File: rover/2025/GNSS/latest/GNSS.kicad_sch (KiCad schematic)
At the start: 34 parts, among them J1 Eth-Horiz, J2 Eth-Horiz, J4 JST6_Pin, J5 USB_C_USB4145-GCT, SW1 TS09-63-25-WT-160-SMT-TR, SW2 TS09-63-25-WT-160-SMT-TR, U1 SN65HVD232, U2 ESP32-S3-WROVER, U3 LDO-LM7805MPX/NOPB, U4 LDO-TLV74033PDBVR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

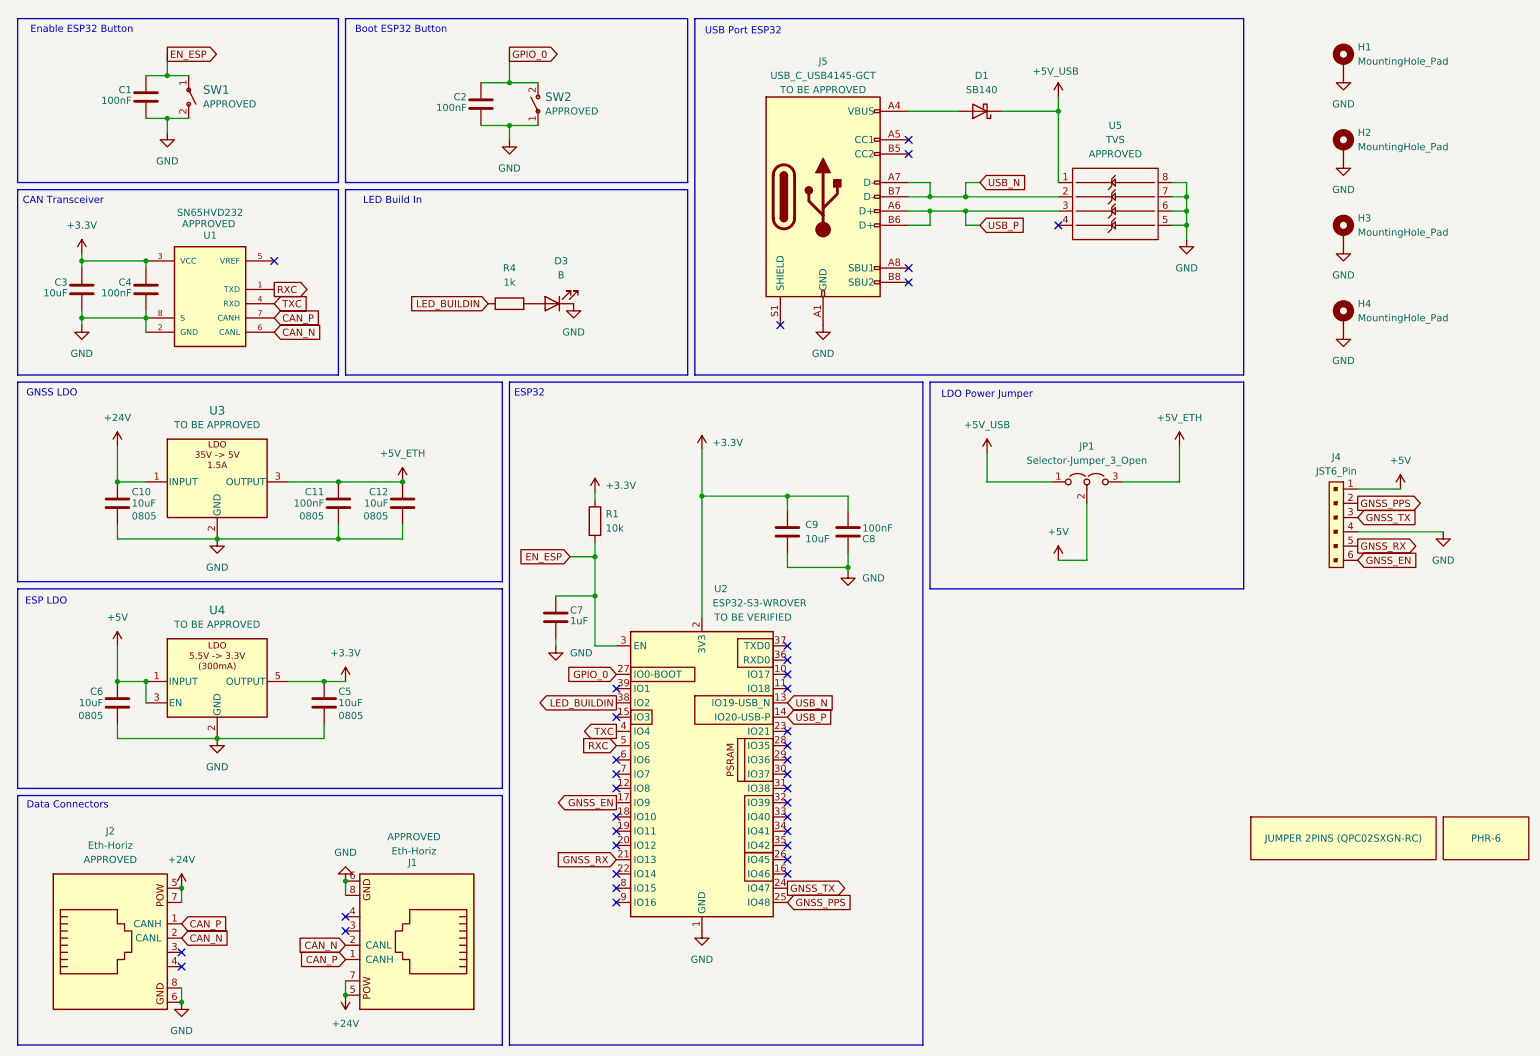
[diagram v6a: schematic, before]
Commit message: GNSS power bug fix
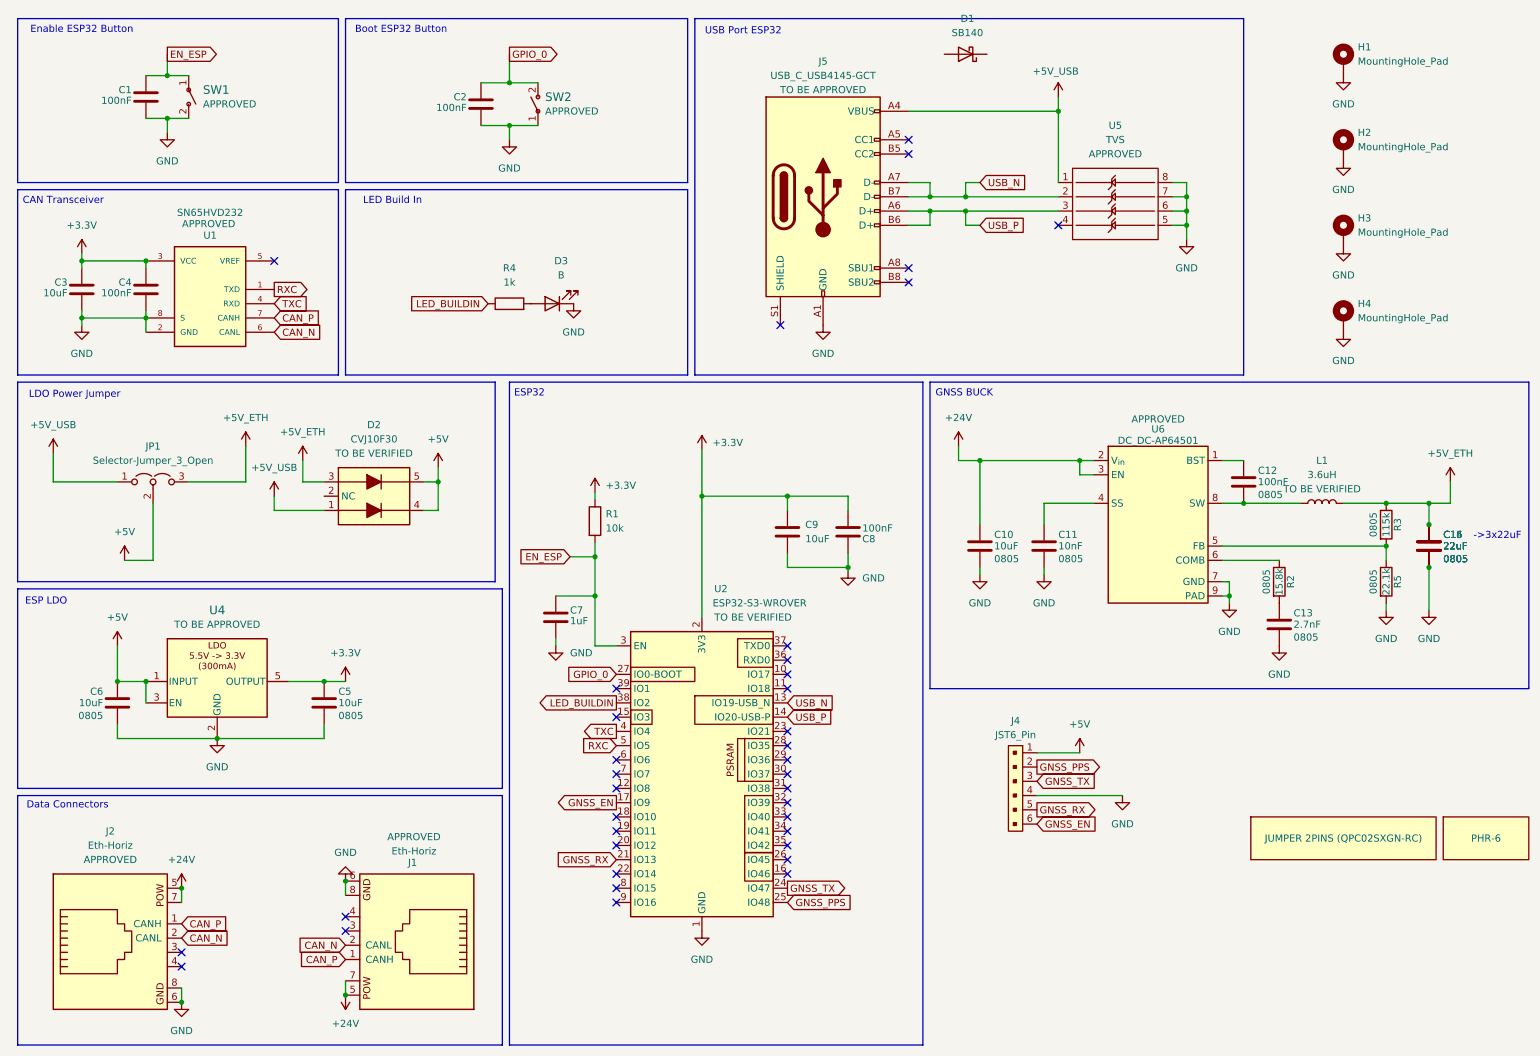
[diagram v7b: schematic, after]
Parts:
- removed C11: 100nF, Capacitor_SMD:C_0805_2012Metric_Pad1.18x1.45mm_HandSolder, symbol Rover_Library:C_0805
- removed U3: LDO-LM7805MPX/NOPB, Package_TO_SOT_SMD:SOT-223-3_TabPin2, symbol RoverLibrary:LDO-LM7805MPX/NOPB
- added C11: 10nF, Capacitor_SMD:C_0805_2012Metric_Pad1.18x1.45mm_HandSolder, symbol RoverLibrary:C_0805
- added C13: 2.7nF, Capacitor_SMD:C_0805_2012Metric_Pad1.18x1.45mm_HandSolder, symbol RoverLibrary:C_0805
- added C14, C15, C16: 22uF, Capacitor_SMD:C_0805_2012Metric_Pad1.18x1.45mm_HandSolder, symbol RoverLibrary:C_0805
- added D2: CVJ10F30, RoverFootprint:Diode_schottky-CVJ10F30, symbol RoverLibrary:Diode_Schottchy_CVJ10F30
- added L1: 3.6uH, RoverFootprint:L_3.6u_ASPI-6045S-3R6N-T, symbol RoverLibrary:L_3.6u_ASPI-6045S-3R6N-T
- added R2: 15.8k, Resistor_SMD:R_0805_2012Metric_Pad1.20x1.40mm_HandSolder, symbol RoverLibrary:R_0805
- added R3: 115k, Resistor_SMD:R_0805_2012Metric_Pad1.20x1.40mm_HandSolder, symbol RoverLibrary:R_0805
- added R5: 22.1k, Resistor_SMD:R_0805_2012Metric_Pad1.20x1.40mm_HandSolder, symbol RoverLibrary:R_0805
- added U6: DC_DC-AP64501, Package_SO:SOIC-8-1EP_3.9x4.9mm_P1.27mm_EP2.29x3mm, symbol RoverLibrary:DC_DC-AP64501
- C12: value 10uF -> 100nF
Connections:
- net +24V: now also U6.2 (V_{in}), U6.3 (EN)
- net +5V: now also D2.4, D2.5
- net +5V_ETH: now also C14.1, C15.1, C16.1, D2.3, L1.2, R3.1; no longer C12.1
- net +5V_USB: now also J5.A4 (VBUS), J5.A9 (VBUS), J5.B4 (VBUS), J5.B9 (VBUS), D2.1; no longer D1.1 (K)
- net GND: now also C11.2, C13.2, C14.2, C15.2, C16.2, R5.2, U6.7 (GND), U6.9 (PAD); no longer C12.2
- removed net VBUS: D1.2 (A), J5.A4 (VBUS), J5.A9 (VBUS), J5.B4 (VBUS), J5.B9 (VBUS)
- new net: C11.1, U6.4 (SS)
- new net: C12.2, L1.1, U6.8 (SW)
- new net: R2.1, U6.6 (COMB)
- new net: C13.1, R2.2
- new net: C12.1, U6.1 (BST)
- new net: R3.2, R5.1, U6.5 (FB)
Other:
- note added: "->3x22uF"
- note added: "GNSS BUCK"
- note removed: "GNSS LDO"
- moved on the sheet: J4, JP1

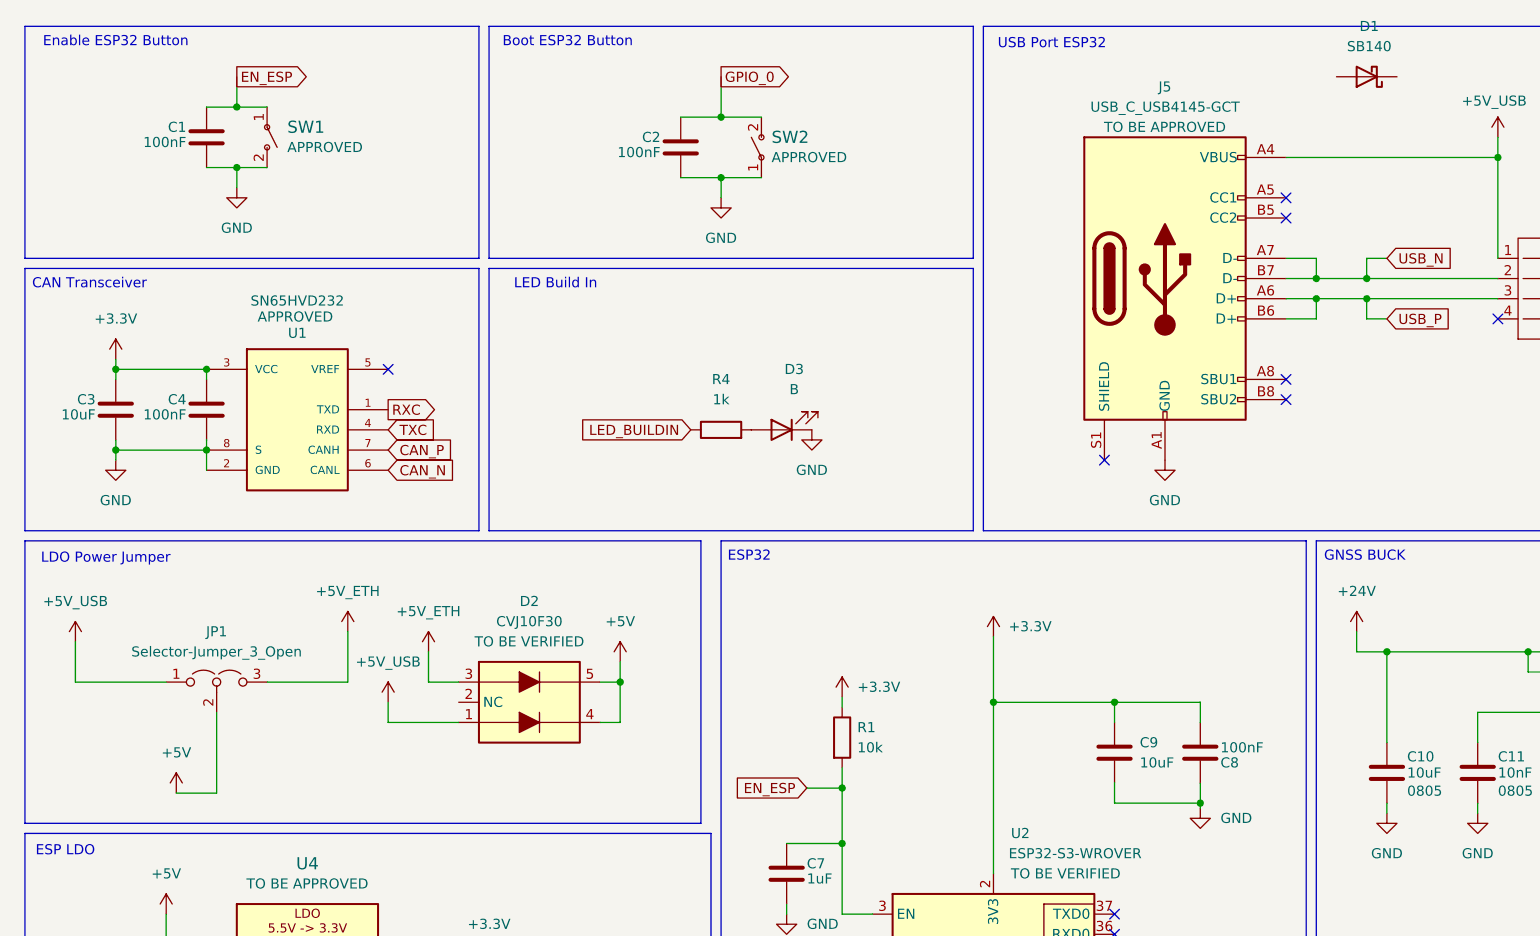
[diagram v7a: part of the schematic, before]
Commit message: gnss modif
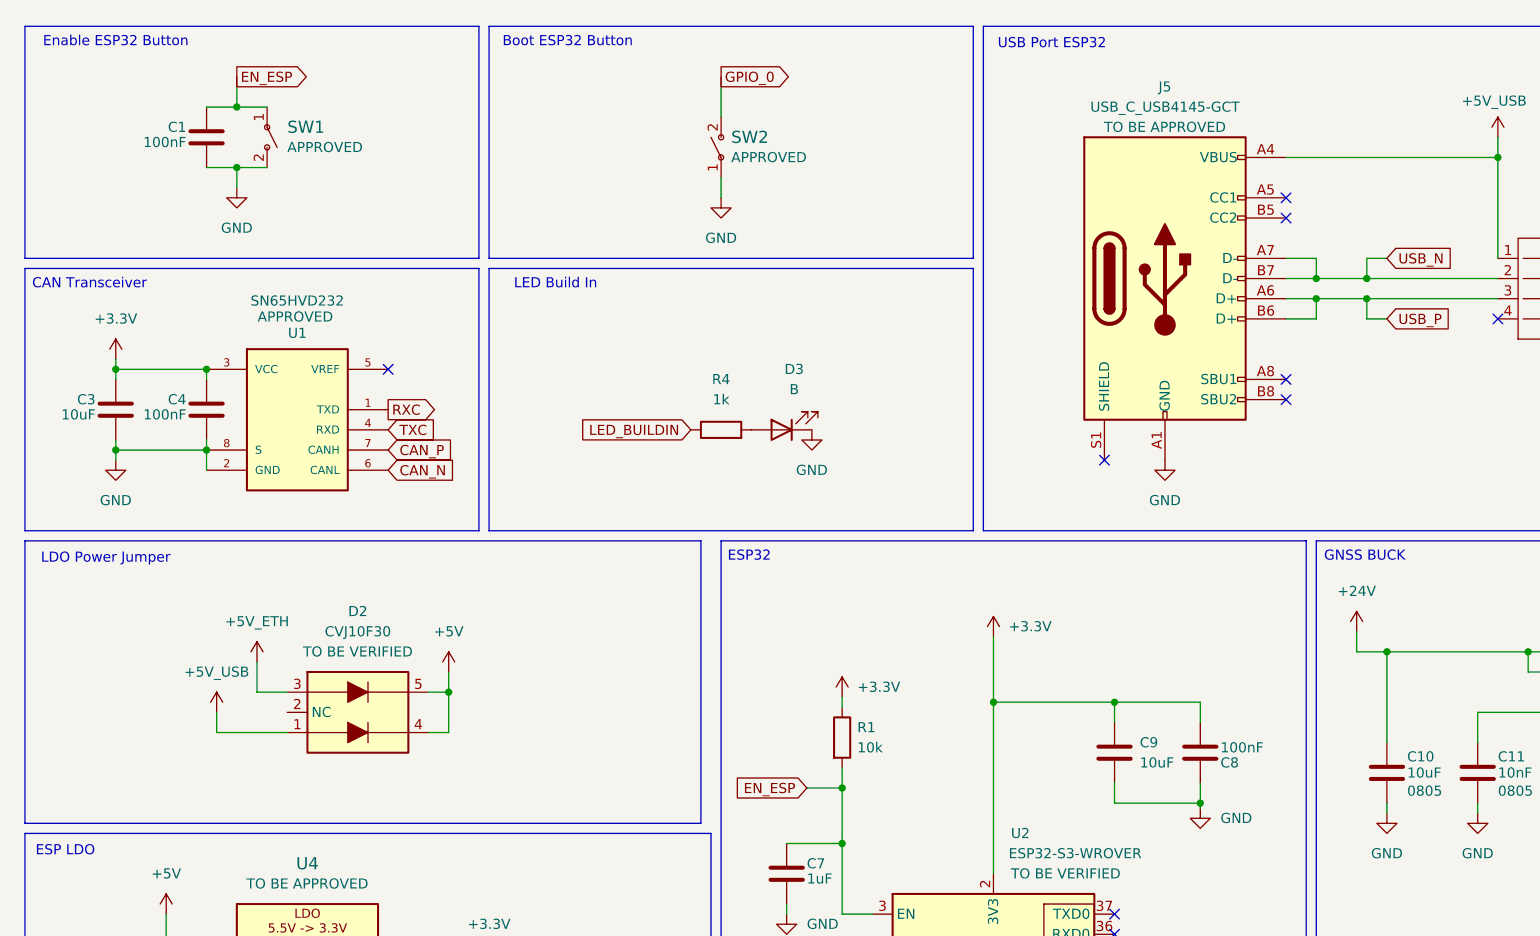
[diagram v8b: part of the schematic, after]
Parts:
- removed C2: 100nF, Capacitor_SMD:C_0805_2012Metric_Pad1.18x1.45mm_HandSolder, symbol RoverLibrary:C-100nF
- removed D1: SB140, Diode_THT:D_DO-41_SOD81_P10.16mm_Horizontal, symbol Diode:SB140
- removed JP1: Selector-Jumper_3_Open, Connector_PinHeader_2.54mm:PinHeader_1x03_P2.54mm_Vertical, symbol RoverLibrary:Selector-Jumper_3_Open
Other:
- moved on the sheet: D2, SW2
